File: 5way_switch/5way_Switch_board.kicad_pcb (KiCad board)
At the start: 2 copper layers, 35 x 22 mm, 8 parts, among them J1 CONN_01X8, SW1 5way-switch

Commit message: More updates. I think we're good.
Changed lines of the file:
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@@
             (gr_line (start -1.012751 -2.540257) (end -2.366089 -2.297148) (width 0.1))
     (gr_arc (start -0.54434 -0.98269) (mid -0.823109 -1.748072) (end -1.012751 -2.540257) (width 0.1))
-    (gr_arc (start -0.18544 2.030115) (mid -1.59044 0.025059) (end -2.366089 -2.297148) (width 0.1))
-    (gr_arc (start 1.829511 0.158474) (mid 1.202376 -0.630683) (end 0.722578 -1.51717) (width 0.1))
+    (gr_arc (start -0.18544 2.030115) (mid -1.587097 0.031686) (end -2.363448 -2.28254) (width 0.1))
+    (gr_arc (start 1.829511 0.158474) (mid 1.205145 -0.626495) (end 0.726574 -1.507958) (width 0.1))
       ))
     (pad "2" smd custom (at -6.9 0 180) (size 1.524 1.524) (layers "B.Cu")
@@
             (xy -1.143 -0.381)
           ) (width 0) (fill yes))
-    (gr_arc (start 1.468521 1.887188) (mid 1.150193 -0.015059) (end 1.478475 -1.915614) (width 0.1))
+    (gr_arc (start 1.468521 1.887188) (mid 1.150193 -0.015059) (end 1.478475 -1.915613) (width 0.1))
             (gr_line (start 1.478475 -1.915614) (end 0.535602 -2.248764) (width 0.1))
             (gr_line (start 0.535602 2.248763) (end 1.478475 1.915613) (width 0.1))
-    (gr_arc (start 0.210716 -0.903391) (mid 0.338493 -1.584449) (end 0.535602 -2.248764) (width 0.1))
+    (gr_arc (start 0.210716 -0.903391) (mid 0.33849 -1.584436) (end 0.535593 -2.248739) (width 0.1))
             (gr_line (start 0.206103 -0.868475) (end -1.529351 -1.093636) (width 0.1))
-    (gr_arc (start -1.533117 1.064237) (mid -1.60006 -0.01482) (end -1.529351 -1.093636) (width 0.1))
+    (gr_arc (start -1.533117 1.064237) (mid -1.60007 -0.007414) (end -1.531246 -1.078946) (width 0.1))
             (gr_line (start -1.529351 1.093635) (end 0.206103 0.868475) (width 0.1))
-    (gr_arc (start 0.527809 2.226602) (mid 0.331665 1.555898) (end 0.206103 0.868475) (width 0.1))
+    (gr_arc (start 0.527809 2.226602) (mid 0.333021 1.561612) (end 0.207621 0.880122) (width 0.1))
             (gr_poly (pts
             (xy 1.478475 1.915613)
@@
             (gr_line (start 1.929527 -0.158491) (end -0.065048 -2.051683) (width 0.1))
             (gr_line (start -2.266089 2.297148) (end -0.912751 2.540256) (width 0.1))
-    (gr_arc (start -0.90831 2.515788) (mid -0.717714 1.730219) (end -0.439415 0.971275) (width 0.1))
-    (gr_arc (start -2.263448 2.282536) (mid -1.480395 -0.044929) (end -0.065048 -2.051683) (width 0.1))
-    (gr_arc (start 0.830582 1.498761) (mid 1.307924 0.622304) (end 1.929527 -0.158491) (width 0.1))
+    (gr_arc (start -0.90831 2.515788) (mid -0.719516 1.736164) (end -0.444337 0.982684) (width 0.1))
+    (gr_arc (start -2.263448 2.282536) (mid -1.483748 -0.03831) (end -0.075253 -2.040908) (width 0.1))
+    (gr_arc (start 0.830582 1.498761) (mid 1.305154 0.626486) (end 1.922628 -0.151208) (width 0.1))
       ))
     (pad "4" smd custom (at -3.8 0 180) (size 1.524 1.524) (layers "B.Cu")
@@
             (gr_line (start 1.139203 2.797621) (end 2.497646 2.584881) (width 0.1))
             (gr_line (start 0.265047 -1.951683) (end -1.729527 -0.058491) (width 0.1))
-    (gr_arc (start 0.285433 -1.930128) (mid 1.732955 0.160094) (end 2.497646 2.584881) (width 0.1))
-    (gr_arc (start 0.712637 1.246919) (mid 0.969948 2.010159) (end 1.139203 2.797621) (width 0.1))
+    (gr_arc (start 0.285433 -1.930128) (mid 1.729688 0.153434) (end 2.495337 2.570226) (width 0.1))
+    (gr_arc (start 0.712637 1.246919) (mid 0.969946 2.010153) (end 1.139201 2.797609) (width 0.1))
     (gr_arc (start -1.715715 -0.043877) (mid -1.063286 0.790947) (end -0.574737 1.731114) (width 0.1))
       ))
@@
           ) (width 0) (fill yes))
             (gr_line (start -0.606104 0.768475) (end 1.129351 0.993635) (width 0.1))
-    (gr_arc (start -0.607622 0.780122) (mid -0.735748 1.473037) (end -0.935602 2.148763) (width 0.1))
+    (gr_arc (start -0.607622 0.780122) (mid -0.735747 1.473031) (end -0.935598 2.148752) (width 0.1))
             (gr_line (start -1.878476 1.815613) (end -0.935602 2.148763) (width 0.1))
-    (gr_arc (start -1.82922 -1.870054) (mid -1.550421 -0.023165) (end -1.878476 1.815613) (width 0.1))
+    (gr_arc (start -1.82922 -1.870054) (mid -1.550356 -0.028181) (end -1.875141 1.806152) (width 0.1))
             (gr_line (start -0.888744 -2.211467) (end -1.83856 -1.898657) (width 0.1))
-    (gr_arc (start 1.151731 -1.004571) (mid 1.199461 -0.004808) (end 1.129351 0.993635) (width 0.1))
+    (gr_arc (start 1.151731 -1.004571) (mid 1.199541 -0.012223) (end 1.131246 0.978926) (width 0.1))
             (gr_line (start 1.151729 -1.004589) (end -0.588333 -0.81835) (width 0.1))
-    (gr_arc (start -0.881411 -2.189057) (mid -0.699254 -1.511319) (end -0.588333 -0.81835) (width 0.1))
+    (gr_arc (start -0.881411 -2.189057) (mid -0.70049 -1.517087) (end -0.589601 -0.83008) (width 0.1))
             (gr_poly (pts
             (xy -0.606104 0.768475)
@@
             (gr_line (start 0.539414 -1.071276) (end -0.722578 -1.61717) (width 0.1))
             (gr_line (start 2.366088 -2.397148) (end 1.01275 -2.640257) (width 0.1))
-    (gr_arc (start -0.734602 -1.589582) (mid -1.210695 -0.71813) (end -1.829527 0.058491) (width 0.1))
-    (gr_arc (start 2.363447 -2.382536) (mid 1.580394 -0.055071) (end 0.165047 1.951683) (width 0.1))
-    (gr_arc (start 1.008309 -2.615789) (mid 0.817713 -1.83022) (end 0.539414 -1.071276) (width 0.1))
+    (gr_arc (start -0.734602 -1.589582) (mid -1.210693 -0.718132) (end -1.829523 0.058487) (width 0.1))
+    (gr_arc (start 2.363447 -2.382536) (mid 1.583747 -0.06169) (end 0.175252 1.940908) (width 0.1))
+    (gr_arc (start 1.008309 -2.615789) (mid 0.819515 -1.836165) (end 0.544336 -1.082685) (width 0.1))
       ))
     (pad "8" smd custom (at 3.7 -0.1 180) (size 1.524 1.524) (layers "B.Cu")

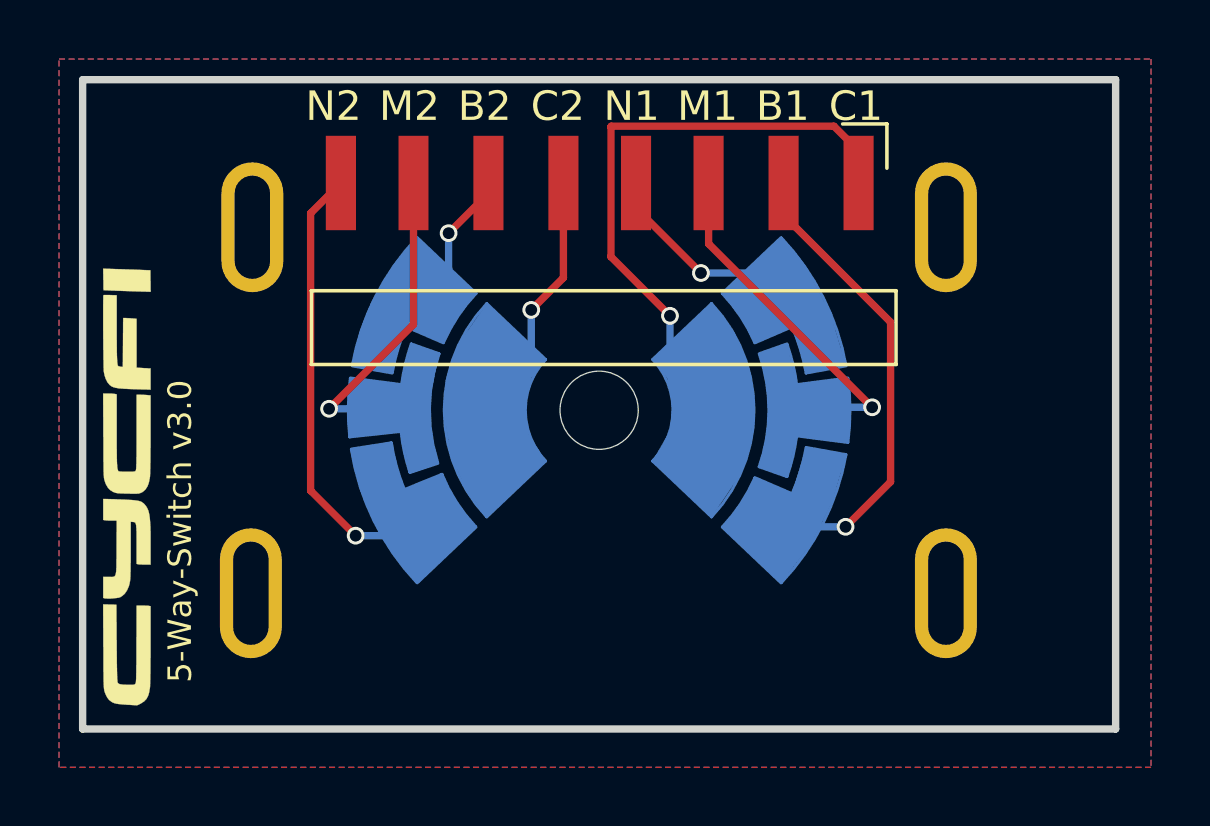
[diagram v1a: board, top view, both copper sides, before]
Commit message: moved the connector closer to the edge
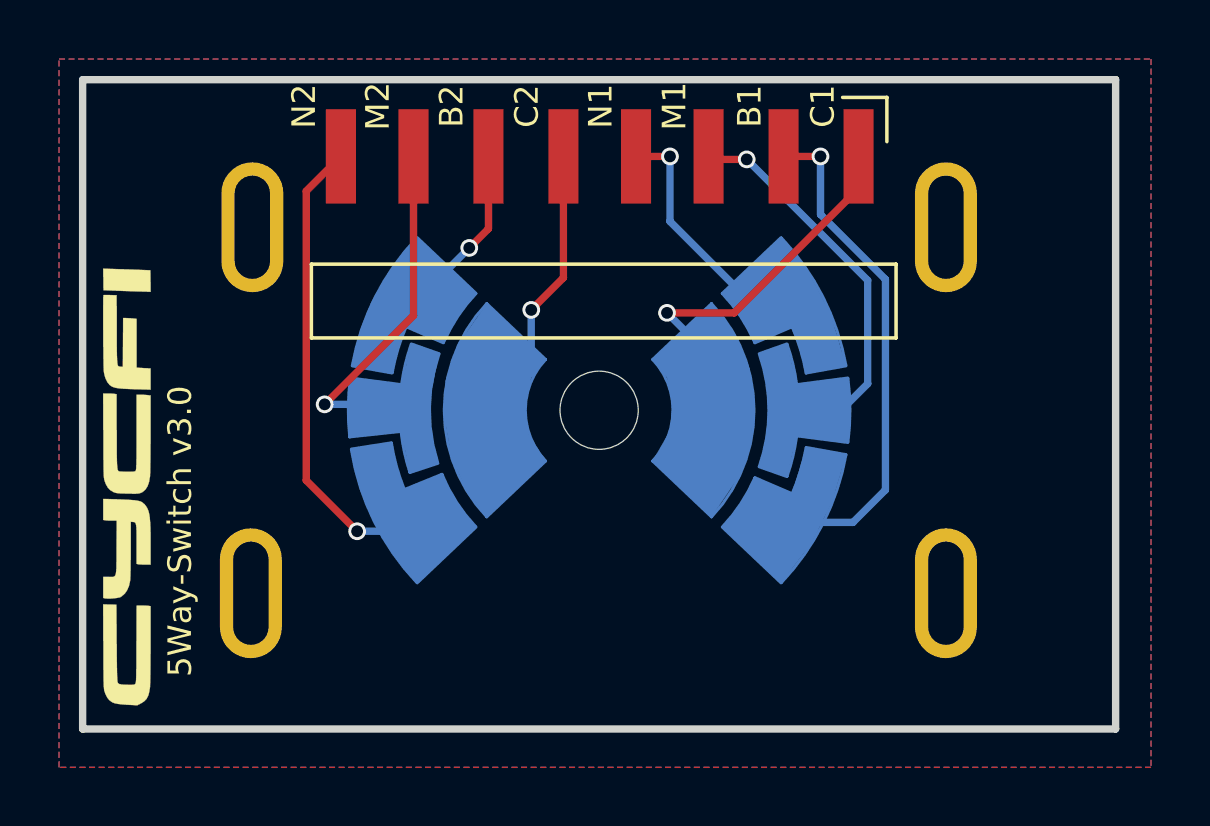
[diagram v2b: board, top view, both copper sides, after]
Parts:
- moved J1 0.90 mm to (165.6, 80.3)
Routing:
- net common1: track 20.8 -> 13.2 mm
- net bridge1: track 16.1 -> 17.5 mm
- net neck1: track 6.86 -> 8.03 mm
- net middle2: track 10.7 -> 11.7 mm
- net middle1: track 12.3 -> 13.2 mm
- net bridge2: track 4.73 -> 5.63 mm
- net common2: track 8.83 -> 9.73 mm
- net neck2: track 15.5 -> 16.3 mm
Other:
- board text added: "5Way-Switch v3.0"
- board text removed: "5-Way-Switch v3.0"
